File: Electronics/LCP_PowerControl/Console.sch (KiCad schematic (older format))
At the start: 1 part, among them J1 Conn_01x06

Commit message: Adding libraries and recent changes
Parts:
- added J?: Conn_02x04_Odd_Even, Connector_PinSocket_2.54mm:PinSocket_2x04_P2.54mm_Vertical, symbol Connector_Generic:Conn_02x04_Odd_Even
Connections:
- net CONSOLE_PWR: now also J?.1 (Pin_1)
- net CONSOLE_RX: now also J?.5 (Pin_5)
- net CONSOLE_TX: now also J?.3 (Pin_3)
- net GND: now also J?.2 (Pin_2), J?.4 (Pin_4), J?.6 (Pin_6), J?.8 (Pin_8)
- no-connect marks 0 -> 1
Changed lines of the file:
@@
 $Descr A4 11693 8268
 encoding utf-8
-Sheet 5 8
+Sheet 4 11
 Title ""
 Date ""
@@
 CONSOLE_TX
 Wire Wire Line
-	6450 3450 3900 3450
+	6450 3450 5500 3450
 Wire Wire Line
-	3900 3550 6450 3550
+	3900 3550 5400 3550
 Text HLabel 6450 3650 2    50   Output ~ 0
 CONSOLE_PWR
 Wire Wire Line
-	6450 3650 3900 3650
+	6450 3650 5300 3650
+$Comp
+L power:GND #PWR?
+U 1 1 5EED83B1
+P 5300 4850
+AR Path="/5EE2AA1B/5EED83B1" Ref="#PWR?"  Part="1"
+AR Path="/5EE2A864/5EED83B1" Ref="#PWR?"  Part="1"
+F 0 "#PWR?" H 5300 4600 50  0001 C CNN
+F 1 "GND" H 5305 4677 50  0000 C CNN
+F 2 "" H 5300 4850 50  0001 C CNN
+F 3 "" H 5300 4850 50  0001 C CNN
+	1    5300 4850
+	1    0    0    -1
+$EndComp
+Wire Wire Line
+	5300 4850 5300 4700
+Wire Wire Line
+	5400 4650 5400 4700
+Wire Wire Line
+	5400 4700 5300 4700
+Connection ~ 5300 4700
+Wire Wire Line
+	5300 4700 5300 4650
+Wire Wire Line
+	5500 4650 5500 4700
+Connection ~ 5400 4700
+$Comp
+L Connector_Generic:Conn_02x04_Odd_Even J?
+U 1 1 5EED83BF
+P 5400 4350
+F 0 "J?" V 5359 4062 50  0000 R CNN
+F 1 "Conn_02x04_Odd_Even" V 5450 4062 50  0000 R CNN
+F 2 "Connector_PinSocket_2.54mm:PinSocket_2x04_P2.54mm_Vertical" H 5400 4350 50  0001 C CNN
+F 3 "~" H 5400 4350 50  0001 C CNN
+F 4 "SALEAE_TEST" V 5541 4062 50  0000 R CNN "Field4"
+	1    5400 4350
+	0    -1   1    0
+$EndComp
+Wire Wire Line
+	5600 4650 5600 4700
+Wire Wire Line
+	5400 4700 5500 4700
+Wire Wire Line
+	5500 4700 5600 4700
+Connection ~ 5500 4700
+Wire Wire Line
+	5300 4150 5300 3650
+Connection ~ 5300 3650
+Wire Wire Line
+	5300 3650 3900 3650
+Wire Wire Line
+	5400 4150 5400 3550
+Connection ~ 5400 3550
+Wire Wire Line
+	5400 3550 6450 3550
+Wire Wire Line
+	5500 4150 5500 3450
+Connection ~ 5500 3450
+Wire Wire Line
+	5500 3450 3900 3450
+NoConn ~ 5600 4150
 $EndSCHEMATC

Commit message: Aiming for rev 0.1 complete
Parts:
- J1: footprint (none) -> Connector_PinSocket_2.54mm:PinSocket_1x06_P2.54mm_Vertical
- gave numbers to parts that had none: 1
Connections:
- no-connect marks 1 -> 3
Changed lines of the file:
@@
 Sheet 4 11
 Title ""
-Date ""
-Rev ""
+Date "2020-06-17"
+Rev "R0.1"
 Comp ""
-Comment1 ""
+Comment1 "Design by: Matt Casari"
 Comment2 ""
 Comment3 ""
@@
 F 0 "J1" H 3618 3125 50  0000 C CNN
 F 1 "Conn_01x06" H 3618 3216 50  0000 C CNN
-F 2 "" H 3700 3650 50  0001 C CNN
+F 2 "Connector_PinSocket_2.54mm:PinSocket_1x06_P2.54mm_Vertical" H 3700 3650 50  0001 C CNN
 F 3 "~" H 3700 3650 50  0001 C CNN
 	1    3700 3650
@@
 	3900 3850 4150 3850
 Wire Wire Line
-	4150 3850 4150 4100
+	4150 3850 4150 3900
 Text HLabel 6450 3450 2    50   Input ~ 0
 CONSOLE_RX
@@
 P 5300 4850
 AR Path="/5EE2AA1B/5EED83B1" Ref="#PWR?"  Part="1"
-AR Path="/5EE2A864/5EED83B1" Ref="#PWR?"  Part="1"
-F 0 "#PWR?" H 5300 4600 50  0001 C CNN
+AR Path="/5EE2A864/5EED83B1" Ref="#PWR033"  Part="1"
+F 0 "#PWR033" H 5300 4600 50  0001 C CNN
 F 1 "GND" H 5305 4677 50  0000 C CNN
 F 2 "" H 5300 4850 50  0001 C CNN
@@
 Connection ~ 5400 4700
 $Comp
-L Connector_Generic:Conn_02x04_Odd_Even J?
+L Connector_Generic:Conn_02x04_Odd_Even J14
 U 1 1 5EED83BF
 P 5400 4350
-F 0 "J?" V 5359 4062 50  0000 R CNN
+F 0 "J14" V 5359 4062 50  0000 R CNN
 F 1 "Conn_02x04_Odd_Even" V 5450 4062 50  0000 R CNN
 F 2 "Connector_PinSocket_2.54mm:PinSocket_2x04_P2.54mm_Vertical" H 5400 4350 50  0001 C CNN
@@
 	5500 3450 3900 3450
 NoConn ~ 5600 4150
+NoConn ~ 3900 3750
+NoConn ~ 3900 3350
+$Comp
+L power:PWR_FLAG #FLG0103
+U 1 1 5EED0A72
+P 4500 3900
+F 0 "#FLG0103" H 4500 3975 50  0001 C CNN
+F 1 "PWR_FLAG" H 4500 4073 50  0000 C CNN
+F 2 "" H 4500 3900 50  0001 C CNN
+F 3 "~" H 4500 3900 50  0001 C CNN
+	1    4500 3900
+	1    0    0    -1
+$EndComp
+Wire Wire Line
+	4150 3900 4500 3900
+Connection ~ 4150 3900
+Wire Wire Line
+	4150 3900 4150 4100
 $EndSCHEMATC

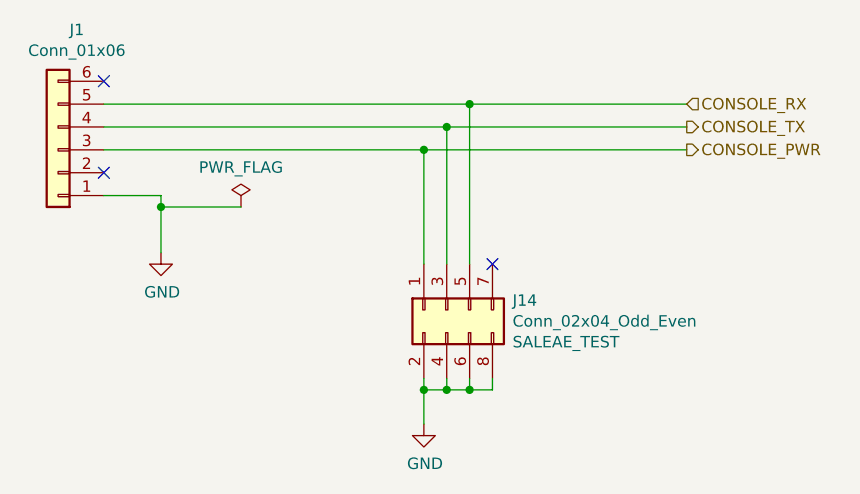
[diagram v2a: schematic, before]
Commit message: Rev1
Removed test points. Cleaned up unnecessary traces. Fixed electrical issues #1-#7
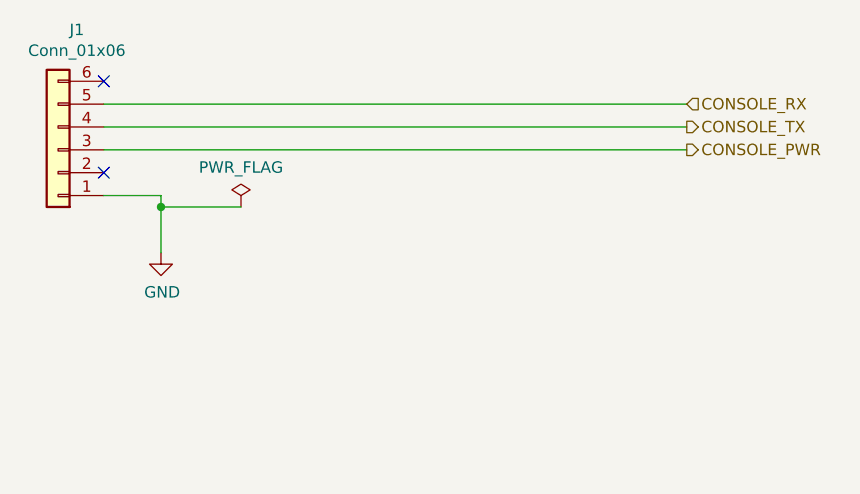
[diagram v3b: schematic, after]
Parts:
- removed J14: Conn_02x04_Odd_Even, Connector_PinSocket_2.54mm:PinSocket_2x04_P2.54mm_Vertical, symbol Connector_Generic:Conn_02x04_Odd_Even
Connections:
- no-connect marks 3 -> 2
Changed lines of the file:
@@
 Text HLabel 6450 3550 2    50   Output ~ 0
 CONSOLE_TX
-Wire Wire Line
-	6450 3450 5500 3450
-Wire Wire Line
-	3900 3550 5400 3550
 Text HLabel 6450 3650 2    50   Output ~ 0
 CONSOLE_PWR
-Wire Wire Line
-	6450 3650 5300 3650
-$Comp
-L power:GND #PWR?
-U 1 1 5EED83B1
-P 5300 4850
-AR Path="/5EE2AA1B/5EED83B1" Ref="#PWR?"  Part="1"
-AR Path="/5EE2A864/5EED83B1" Ref="#PWR033"  Part="1"
-F 0 "#PWR033" H 5300 4600 50  0001 C CNN
-F 1 "GND" H 5305 4677 50  0000 C CNN
-F 2 "" H 5300 4850 50  0001 C CNN
-F 3 "" H 5300 4850 50  0001 C CNN
-	1    5300 4850
-	1    0    0    -1
-$EndComp
-Wire Wire Line
-	5300 4850 5300 4700
-Wire Wire Line
-	5400 4650 5400 4700
-Wire Wire Line
-	5400 4700 5300 4700
-Connection ~ 5300 4700
-Wire Wire Line
-	5300 4700 5300 4650
-Wire Wire Line
-	5500 4650 5500 4700
-Connection ~ 5400 4700
-$Comp
-L Connector_Generic:Conn_02x04_Odd_Even J14
-U 1 1 5EED83BF
-P 5400 4350
-F 0 "J14" V 5359 4062 50  0000 R CNN
-F 1 "Conn_02x04_Odd_Even" V 5450 4062 50  0000 R CNN
-F 2 "Connector_PinSocket_2.54mm:PinSocket_2x04_P2.54mm_Vertical" H 5400 4350 50  0001 C CNN
-F 3 "~" H 5400 4350 50  0001 C CNN
-F 4 "SALEAE_TEST" V 5541 4062 50  0000 R CNN "Field4"
-	1    5400 4350
-	0    -1   1    0
-$EndComp
-Wire Wire Line
-	5600 4650 5600 4700
-Wire Wire Line
-	5400 4700 5500 4700
-Wire Wire Line
-	5500 4700 5600 4700
-Connection ~ 5500 4700
-Wire Wire Line
-	5300 4150 5300 3650
-Connection ~ 5300 3650
-Wire Wire Line
-	5300 3650 3900 3650
-Wire Wire Line
-	5400 4150 5400 3550
-Connection ~ 5400 3550
-Wire Wire Line
-	5400 3550 6450 3550
-Wire Wire Line
-	5500 4150 5500 3450
-Connection ~ 5500 3450
-Wire Wire Line
-	5500 3450 3900 3450
-NoConn ~ 5600 4150
 NoConn ~ 3900 3750
 NoConn ~ 3900 3350
@@
 Wire Wire Line
 	4150 3900 4150 4100
+Wire Wire Line
+	3900 3650 6450 3650
+Wire Wire Line
+	3900 3550 6450 3550
+Wire Wire Line
+	3900 3450 6450 3450
 $EndSCHEMATC

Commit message: BOM Update
Updated MPNs on components to match supplies as well as correcting some resistor values
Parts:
- J1: MPN (none) -> 61300611121
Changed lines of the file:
@@
 F 2 "Connector_PinSocket_2.54mm:PinSocket_1x06_P2.54mm_Vertical" H 3700 3650 50  0001 C CNN
 F 3 "~" H 3700 3650 50  0001 C CNN
+F 4 "61300611121" H 3700 3650 50  0001 C CNN "MPN"
 	1    3700 3650
 	-1   0    0    1
